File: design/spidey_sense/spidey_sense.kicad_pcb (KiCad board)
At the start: 2 copper layers, 63.5 x 46.5 mm, 10 parts, among them J1 Input_Screw_Terminal, J10 Output_Screw_Terminal, J2 Thermocouple_Terminal, J3 Thermocouple_Terminal, J4 Thermocouple_Terminal, J5 Thermocouple_Terminal, J6 Conn_01x06_Female, J7 Conn_01x06_Female, J8 Conn_01x06_Female, J9 Conn_01x06_Female

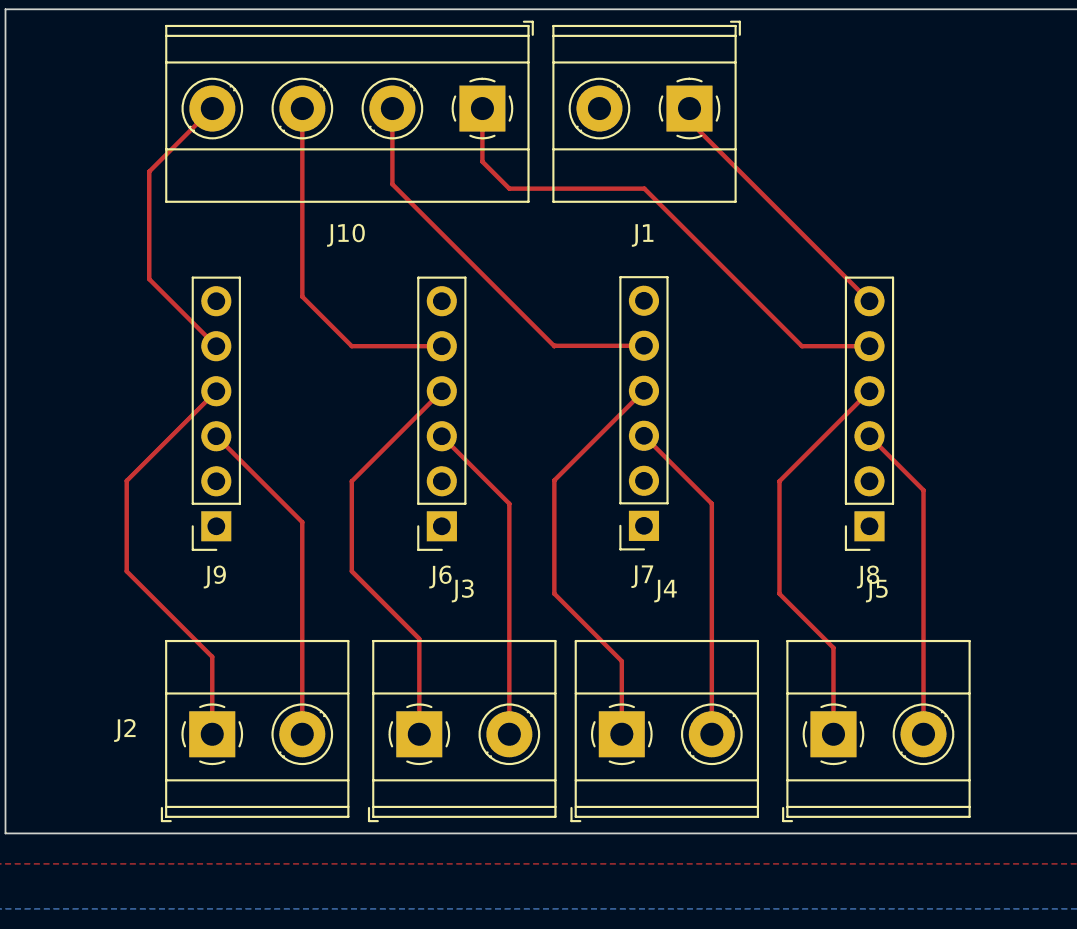
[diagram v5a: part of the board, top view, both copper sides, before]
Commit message: Changed component orientations and added labels
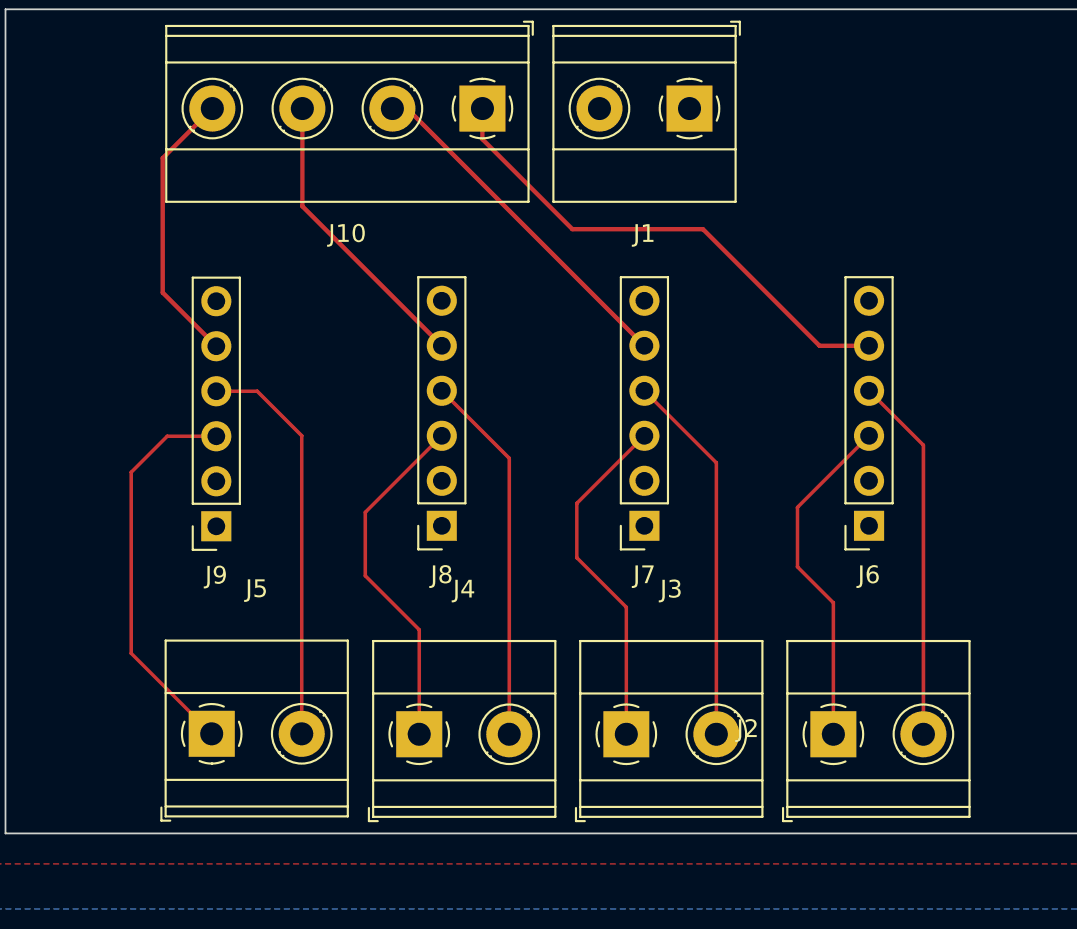
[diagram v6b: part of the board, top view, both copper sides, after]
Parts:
- moved J9 36.9 mm to (58.4, 90.2)
- moved J6 36.8 mm to (95.2, 90.1)
- moved J5 35.1 mm to (58.1, 101.9)
- moved J2 35.0 mm to (93.2, 101.9)
- moved J3 11.7 mm to (81.5, 101.9)
- moved J7 11.4 mm to (82.5, 90.1)
- moved J4 11.4 mm to (69.8, 101.9)
- moved J8 11.4 mm to (71.1, 90.1)
- renumbered J9 to J6, J6 to J7, J7 to J8, J8 to J9
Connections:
- J1 pad 1: GND -> +24V
- J1 pad 2: +24V -> GND
- J10 pad 1: Net-(J8-Pad5) -> /Aout
- J10 pad 2: Net-(J7-Pad5) -> /Bout
- J10 pad 3: Net-(J6-Pad5) -> /Cout
- J10 pad 4: Net-(J10-Pad4) -> /Dout
- J2 pad 1: Net-(J2-Pad1) -> /A+
- J2 pad 2: Net-(J2-Pad2) -> /A-
- J3 pad 1: Net-(J3-Pad1) -> /B+
- J3 pad 2: Net-(J3-Pad2) -> /B-
- J4 pad 1: Net-(J4-Pad1) -> /C+
- J4 pad 2: Net-(J4-Pad2) -> /C-
- J5 pad 1: Net-(J5-Pad1) -> /D+
- J5 pad 2: Net-(J5-Pad2) -> /D-
- J6 pad 3: Net-(J2-Pad2) -> /A+
- J6 pad 4: Net-(J2-Pad1) -> /A-
- J6 pad 5: Net-(J10-Pad4) -> /Aout
- J7 pad 3: Net-(J3-Pad2) -> /B+
- J7 pad 4: Net-(J3-Pad1) -> /B-
- J7 pad 5: Net-(J6-Pad5) -> /Bout
- J8 pad 3: Net-(J4-Pad2) -> /C+
- J8 pad 4: Net-(J4-Pad1) -> /C-
- J8 pad 5: Net-(J7-Pad5) -> /Cout
- J9 pad 3: Net-(J5-Pad2) -> /D+
- J9 pad 4: Net-(J5-Pad1) -> /D-
- J9 pad 5: Net-(J8-Pad5) -> /Dout
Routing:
- net Net-(J8-Pad5): track 29.2 -> 0.00 mm
- net /Aout: track 0.00 -> 28.4 mm
- net Net-(J2-Pad1): track 23.4 -> 0.00 mm
- net Net-(J4-Pad1): track 23.0 -> 0.00 mm
- net Net-(J3-Pad1): track 23.0 -> 0.00 mm
- net Net-(J5-Pad1): track 22.7 -> 0.00 mm
- net /D-: track 0.00 -> 22.7 mm
- net /D+: track 0.00 -> 22.3 mm
- net Net-(J7-Pad5): track 22.3 -> 0.00 mm
- net /B-: track 0.00 -> 21.1 mm
- net /C-: track 0.00 -> 21.0 mm
- net /A-: track 0.00 -> 20.7 mm
- net /C+: track 0.00 -> 19.9 mm
- net /Bout: track 0.00 -> 19.8 mm
- net Net-(J6-Pad5): track 19.6 -> 0.00 mm
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
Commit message: Initial PCB design
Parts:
- added REF**: MountingHole_3.2mm_M3_Pad, MountingHole:MountingHole_3.2mm_M3_Pad, F.Cu at (105.4, 66.5)
- added REF**: MountingHole_3.2mm_M3_Pad, MountingHole:MountingHole_3.2mm_M3_Pad, F.Cu at (50.5, 101.6)
- added REF**: MountingHole_3.2mm_M3_Pad, MountingHole:MountingHole_3.2mm_M3_Pad, F.Cu at (105.7, 101.6)
- added REF**: MountingHole_3.2mm_M3_Pad, MountingHole:MountingHole_3.2mm_M3_Pad, F.Cu at (51.1, 66.0)
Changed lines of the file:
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@@
     (property "Sheetname" "")
     (attr through_hole)
-    (fp_text reference "J7" (at 0 -2.77) (layer "F.SilkS")
+    (fp_text reference "J7" (at 3.048 7.595) (layer "F.SilkS")
       (effects (font (size 1 1) (thickness 0.15)))
     )
@@
     )
   )
+  (footprint "MountingHole:MountingHole_3.2mm_M3_Pad" (layer "F.Cu")
+    (at 105.41 66.548)
+    (descr "Mounting Hole 3.2mm, M3")
+    (tags "mounting hole 3.2mm m3")
+    (attr exclude_from_pos_files exclude_from_bom)
+    (fp_text reference "REF**" (at 0 -4.2) (layer "F.SilkS")
+      (effects (font (size 1 1) (thickness 0.15)))
+    )
+    (fp_text value "MountingHole_3.2mm_M3_Pad" (at 0 4.2) (layer "F.Fab")
+      (effects (font (size 1 1) (thickness 0.15)))
+    )
+    (fp_text user "${REFERENCE}" (at 0 0) (layer "F.Fab")
+      (effects (font (size 1 1) (thickness 0.15)))
+    )
+    (fp_circle (center 0 0) (end 3.2 0) (layer "Cmts.User") (width 0.15) (fill none))
+    (fp_circle (center 0 0) (end 3.45 0) (layer "F.CrtYd") (width 0.05) (fill none))
+    (pad "1" thru_hole circle (at 0 0) (size 6.4 6.4) (drill 3.2) (layers *.Cu *.Mask))
+  )
   (footprint "Connector_PinSocket_2.54mm:PinSocket_1x06_P2.54mm_Vertical" (layer "F.Cu")
     (at 71.12 90.145 180)
@@
     (property "Sheetname" "")
     (attr through_hole)
-    (fp_text reference "J8" (at 0 -2.77) (layer "F.SilkS")
+    (fp_text reference "J8" (at 3.048 7.595) (layer "F.SilkS")
       (effects (font (size 1 1) (thickness 0.15)))
     )
@@
     (property "Sheetname" "")
     (attr through_hole)
-    (fp_text reference "J3" (at 2.54 -8.179) (layer "F.SilkS")
+    (fp_text reference "J3" (at 2.54 -6.655) (layer "F.SilkS")
       (effects (font (size 1 1) (thickness 0.15)))
     )
@@
     (property "Sheetname" "")
     (attr through_hole)
-    (fp_text reference "J1" (at 2.545 -7.06) (layer "F.SilkS")
+    (fp_text reference "J1" (at -4.567 -0.456) (layer "F.SilkS")
       (effects (font (size 1 1) (thickness 0.15)))
     )
@@
     (property "Sheetname" "")
     (attr through_hole)
-    (fp_text reference "J2" (at -4.826 -0.305) (layer "F.SilkS")
+    (fp_text reference "J2" (at 2.799 -6.655) (layer "F.SilkS")
       (effects (font (size 1 1) (thickness 0.15)))
     )
@@
     )
   )
+  (footprint "MountingHole:MountingHole_3.2mm_M3_Pad" (layer "F.Cu")
+    (at 50.546 101.6)
+    (descr "Mounting Hole 3.2mm, M3")
+    (tags "mounting hole 3.2mm m3")
+    (attr exclude_from_pos_files exclude_from_bom)
+    (fp_text reference "REF**" (at 0 -4.2) (layer "F.SilkS")
+      (effects (font (size 1 1) (thickness 0.15)))
+    )
+    (fp_text value "MountingHole_3.2mm_M3_Pad" (at 0 4.2) (layer "F.Fab")
+      (effects (font (size 1 1) (thickness 0.15)))
+    )
+    (fp_text user "${REFERENCE}" (at 0 0) (layer "F.Fab")
+      (effects (font (size 1 1) (thickness 0.15)))
+    )
+    (fp_circle (center 0 0) (end 3.2 0) (layer "Cmts.User") (width 0.15) (fill none))
+    (fp_circle (center 0 0) (end 3.45 0) (layer "F.CrtYd") (width 0.05) (fill none))
+    (pad "1" thru_hole circle (at 0 0) (size 6.4 6.4) (drill 3.2) (layers *.Cu *.Mask))
+  )
   (footprint "TerminalBlock_Phoenix:TerminalBlock_Phoenix_MKDS-1,5-4-5.08_1x04_P5.08mm_Horizontal" (layer "F.Cu")
     (at 73.411 66.6 180)
@@
     (property "Sheetname" "")
     (attr through_hole)
-    (fp_text reference "J10" (at 7.62 -7.06) (layer "F.SilkS")
+    (fp_text reference "J10" (at 3.561 -7.822) (layer "F.SilkS")
       (effects (font (size 1 1) (thickness 0.15)))
     )
@@
     (property "Sheetname" "")
     (attr through_hole)
-    (fp_text reference "J9" (at 0 -2.77) (layer "F.SilkS")
+    (fp_text reference "J9" (at 2.769 7.62) (layer "F.SilkS")
       (effects (font (size 1 1) (thickness 0.15)))
     )
@@
     (property "Sheetname" "")
     (attr through_hole)
-    (fp_text reference "J6" (at 0 -2.77) (layer "F.SilkS")
+    (fp_text reference "J6" (at 2.769 7.341) (layer "F.SilkS")
       (effects (font (size 1 1) (thickness 0.15)))
     )
@@
     )
   )
+  (footprint "MountingHole:MountingHole_3.2mm_M3_Pad" (layer "F.Cu")
+    (at 105.664 101.6)
+    (descr "Mounting Hole 3.2mm, M3")
+    (tags "mounting hole 3.2mm m3")
+    (attr exclude_from_pos_files exclude_from_bom)
+    (fp_text reference "REF**" (at 0 -4.2) (layer "F.SilkS")
+      (effects (font (size 1 1) (thickness 0.15)))
+    )
+    (fp_text value "MountingHole_3.2mm_M3_Pad" (at 0 4.2) (layer "F.Fab")
+      (effects (font (size 1 1) (thickness 0.15)))
+    )
+    (fp_text user "${REFERENCE}" (at 0 0) (layer "F.Fab")
+      (effects (font (size 1 1) (thickness 0.15)))
+    )
+    (fp_circle (center 0 0) (end 3.2 0) (layer "Cmts.User") (width 0.15) (fill none))
+    (fp_circle (center 0 0) (end 3.45 0) (layer "F.CrtYd") (width 0.05) (fill none))
+    (pad "1" thru_hole circle (at 0 0) (size 6.4 6.4) (drill 3.2) (layers *.Cu *.Mask))
+  )
+  (footprint "MountingHole:MountingHole_3.2mm_M3_Pad" (layer "F.Cu")
+    (at 51.054 66.04)
+    (descr "Mounting Hole 3.2mm, M3")
+    (tags "mounting hole 3.2mm m3")
+    (attr exclude_from_pos_files exclude_from_bom)
+    (fp_text reference "REF**" (at 0 -4.2) (layer "F.SilkS")
+      (effects (font (size 1 1) (thickness 0.15)))
+    )
+    (fp_text value "MountingHole_3.2mm_M3_Pad" (at 0 4.2) (layer "F.Fab")
+      (effects (font (size 1 1) (thickness 0.15)))
+    )
+    (fp_text user "${REFERENCE}" (at 0 0) (layer "F.Fab")
+      (effects (font (size 1 1) (thickness 0.15)))
+    )
+    (fp_circle (center 0 0) (end 3.2 0) (layer "Cmts.User") (width 0.15) (fill none))
+    (fp_circle (center 0 0) (end 3.45 0) (layer "F.CrtYd") (width 0.05) (fill none))
+    (pad "1" thru_hole circle (at 0 0) (size 6.4 6.4) (drill 3.2) (layers *.Cu *.Mask))
+  )
   (footprint "TerminalBlock_Phoenix:TerminalBlock_Phoenix_MKDS-1,5-2-5.08_1x02_P5.08mm_Horizontal" (layer "F.Cu")
     (at 58.1356 101.8796)
@@
     (property "Sheetname" "")
     (attr through_hole)
-    (fp_text reference "J5" (at 2.54 -8.179) (layer "F.SilkS")
+    (fp_text reference "J5" (at 2.3164 -6.6296) (layer "F.SilkS")
       (effects (font (size 1 1) (thickness 0.15)))
     )
@@
     (property "Sheetname" "")
     (attr through_hole)
-    (fp_text reference "J4" (at 2.54 -8.179) (layer "F.SilkS")
-      (effects (font (size 1 1) (thickness 0.15)))
-    )
+    (fp_text reference "J4" (at 2.54 -6.655) (layer "F.SilkS")
+      (effects (font (size 1 1) (thickness 0.15)))
+    )
